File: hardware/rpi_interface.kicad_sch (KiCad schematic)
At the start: 5 parts, among them J14 RPI_Connector, M1 Noctua NF-A4x10

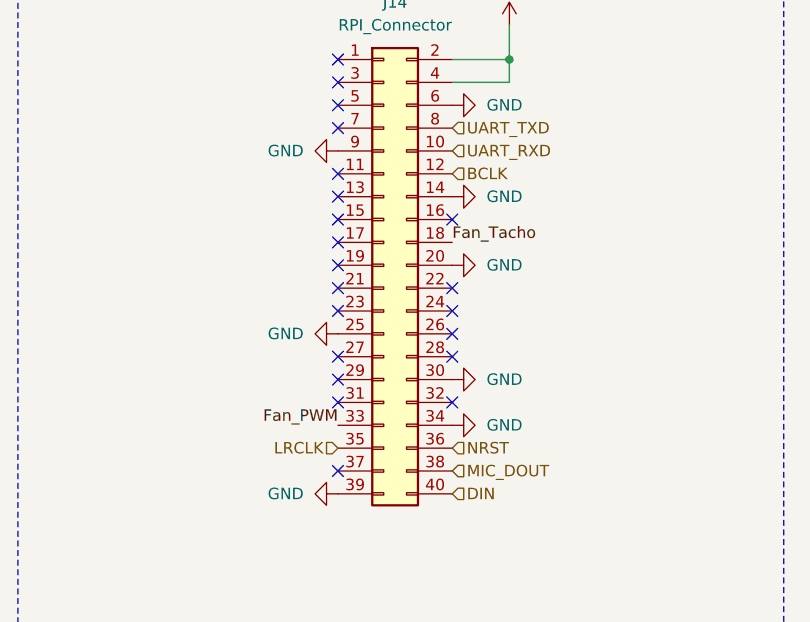
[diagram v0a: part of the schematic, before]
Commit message: schematic update
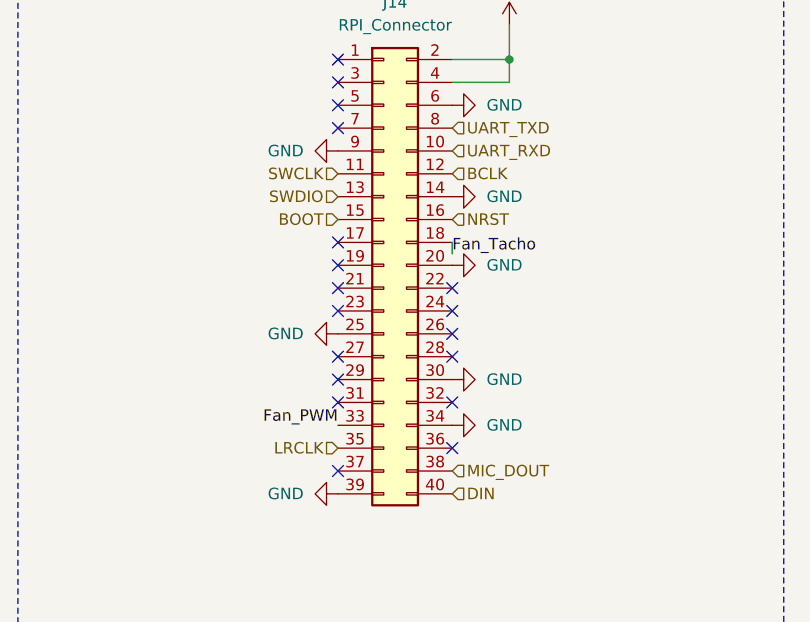
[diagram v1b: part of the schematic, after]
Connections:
- net NRST: now also J14.16 (Pin_16); no longer J14.36 (Pin_36)
- net SWCLK: now reaches J14.11 (Pin_11)
- net SWDIO: now reaches J14.13 (Pin_13)
- net BOOT: now reaches J14.15 (Pin_15)
- no-connect marks 21 -> 18
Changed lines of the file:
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@@
 	)
 	(no_connect
-		(at 142.24 90.17)
+		(at 154.94 120.65)
 	)
 	(no_connect
@@
 	)
 	(no_connect
-		(at 154.94 95.25)
-	)
-	(no_connect
 		(at 142.24 100.33)
 	)
@@
 	)
 	(no_connect
-		(at 142.24 92.71)
-	)
-	(no_connect
 		(at 142.24 123.19)
 	)
@@
 	)
 	(no_connect
-		(at 142.24 95.25)
-	)
-	(no_connect
 		(at 154.94 107.95)
 	)
@@
 	(wire
 		(pts
+			(xy 154.94 99.06) (xy 154.94 97.79)
+		)
+		(stroke
+			(width 0)
+			(type default)
+		)
+	)
+	(wire
+		(pts
 			(xy 209.55 118.11) (xy 212.09 118.11)
 		)
@@
 	)
 	(label "Fan_Tacho"
-		(at 154.94 97.79 0)
+		(at 154.94 99.06 0)
 		(effects
 			(font
@@
 		)
 	)
-	(hierarchical_label "NRST"
+	(hierarchical_label "MIC_DOUT"
 		(shape input)
-		(at 154.94 120.65 0)
+		(at 154.94 123.19 0)
 		(effects
 			(font
@@
 		)
 	)
-	(hierarchical_label "MIC_DOUT"
+	(hierarchical_label "UART_RXD"
 		(shape input)
-		(at 154.94 123.19 0)
+		(at 154.94 87.63 0)
 		(effects
 			(font
@@
 		)
 	)
-	(hierarchical_label "UART_RXD"
+	(hierarchical_label "DIN"
 		(shape input)
-		(at 154.94 87.63 0)
+		(at 154.94 125.73 0)
 		(effects
 			(font
@@
 		)
 	)
-	(hierarchical_label "DIN"
+	(hierarchical_label "SWDIO"
 		(shape input)
-		(at 154.94 125.73 0)
+		(at 142.24 92.71 180)
 		(effects
 			(font
 				(size 1.27 1.27)
 			)
-			(justify left)
+			(justify right)
 		)
 	)
@@
 		)
 	)
+	(hierarchical_label "SWCLK"
+		(shape input)
+		(at 142.24 90.17 180)
+		(effects
+			(font
+				(size 1.27 1.27)
+			)
+			(justify right)
+		)
+	)
 	(hierarchical_label "UART_TXD"
 		(shape input)
@@
 		)
 	)
+	(hierarchical_label "NRST"
+		(shape input)
+		(at 154.94 95.25 0)
+		(effects
+			(font
+				(size 1.27 1.27)
+			)
+			(justify left)
+		)
+	)
+	(hierarchical_label "BOOT"
+		(shape input)
+		(at 142.24 95.25 180)
+		(effects
+			(font
+				(size 1.27 1.27)
+			)
+			(justify right)
+		)
+	)

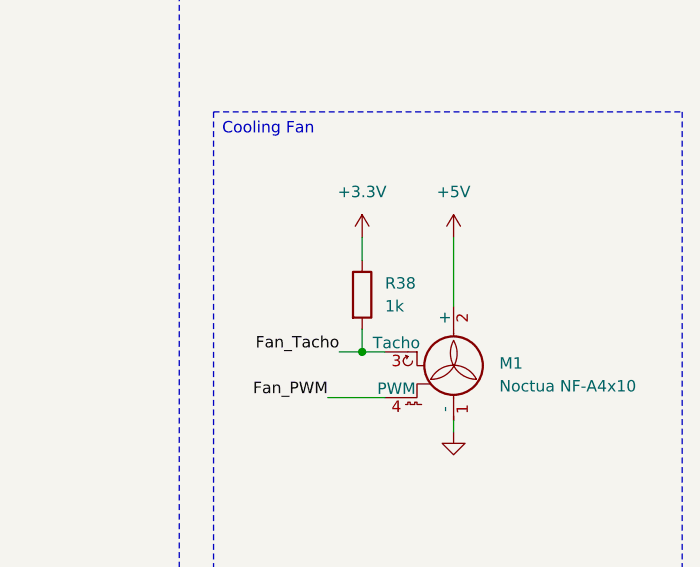
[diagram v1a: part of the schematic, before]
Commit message: replacing components
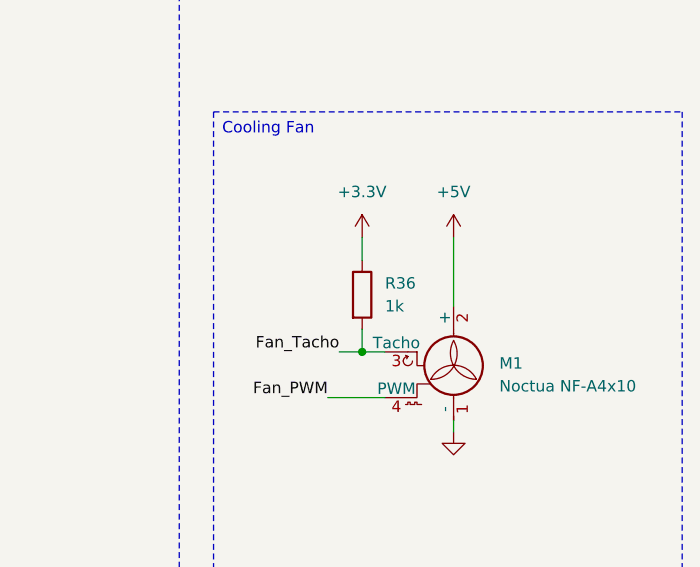
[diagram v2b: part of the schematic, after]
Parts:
- renumbered R38 to R36
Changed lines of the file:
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@@
 		(dnp no)
 		(fields_autoplaced yes)
-		(property "Reference" "#PWR0107"
+		(property "Reference" "#PWR0101"
 			(at 161.29 92.71 0)
 			(hide yes)
@@
 			(project "chromapi_motherboard_v1"
 				(path "/d1a31f26-03e0-43e1-89c1-031fe31befc5/e996aba6-741c-4e73-a7c7-e6548b7ec52f"
-					(reference "#PWR0107")
+					(reference "#PWR0101")
 					(unit 1)
 				)
@@
 		(dnp no)
 		(fields_autoplaced yes)
-		(property "Reference" "#PWR0117"
+		(property "Reference" "#PWR0111"
 			(at 222.25 133.35 0)
 			(hide yes)
@@
 			(project "chromapi_motherboard_v1"
 				(path "/d1a31f26-03e0-43e1-89c1-031fe31befc5/e996aba6-741c-4e73-a7c7-e6548b7ec52f"
-					(reference "#PWR0117")
+					(reference "#PWR0111")
 					(unit 1)
 				)
@@
 		(dnp no)
 		(fields_autoplaced yes)
-		(property "Reference" "#PWR0115"
+		(property "Reference" "#PWR0109"
 			(at 71.12 130.81 0)
 			(hide yes)
@@
 			(project "chromapi_motherboard_v1"
 				(path "/d1a31f26-03e0-43e1-89c1-031fe31befc5/e996aba6-741c-4e73-a7c7-e6548b7ec52f"
-					(reference "#PWR0115")
+					(reference "#PWR0109")
 					(unit 1)
 				)
@@
 		(dnp no)
 		(fields_autoplaced yes)
-		(property "Reference" "#PWR0106"
+		(property "Reference" "#PWR0100"
 			(at 135.89 87.63 0)
 			(hide yes)
@@
 			(project "chromapi_motherboard_v1"
 				(path "/d1a31f26-03e0-43e1-89c1-031fe31befc5/e996aba6-741c-4e73-a7c7-e6548b7ec52f"
-					(reference "#PWR0106")
+					(reference "#PWR0100")
 					(unit 1)
 				)
@@
 		(dnp no)
 		(fields_autoplaced yes)
-		(property "Reference" "R38"
+		(property "Reference" "R36"
 			(at 214.63 110.4899 0)
 			(show_name no)
@@
 			(project "chromapi_motherboard_v1"
 				(path "/d1a31f26-03e0-43e1-89c1-031fe31befc5/e996aba6-741c-4e73-a7c7-e6548b7ec52f"
-					(reference "R38")
+					(reference "R36")
 					(unit 1)
 				)
@@
 		(in_pos_files yes)
 		(dnp no)
-		(property "Reference" "#PWR0111"
+		(property "Reference" "#PWR0105"
 			(at 71.12 111.76 0)
 			(hide yes)
@@
 			(project "chromapi_motherboard_v1"
 				(path "/d1a31f26-03e0-43e1-89c1-031fe31befc5/e996aba6-741c-4e73-a7c7-e6548b7ec52f"
-					(reference "#PWR0111")
+					(reference "#PWR0105")
 					(unit 1)
 				)
@@
 		(dnp no)
 		(fields_autoplaced yes)
-		(property "Reference" "#PWR0116"
+		(property "Reference" "#PWR0110"
 			(at 135.89 125.73 0)
 			(hide yes)
@@
 			(project "chromapi_motherboard_v1"
 				(path "/d1a31f26-03e0-43e1-89c1-031fe31befc5/e996aba6-741c-4e73-a7c7-e6548b7ec52f"
-					(reference "#PWR0116")
+					(reference "#PWR0110")
 					(unit 1)
 				)
@@
 		(dnp no)
 		(fields_autoplaced yes)
-		(property "Reference" "#PWR0104"
+		(property "Reference" "#PWR098"
 			(at 161.29 77.47 0)
 			(hide yes)
@@
 			(project "chromapi_motherboard_v1"
 				(path "/d1a31f26-03e0-43e1-89c1-031fe31befc5/e996aba6-741c-4e73-a7c7-e6548b7ec52f"
-					(reference "#PWR0104")
+					(reference "#PWR098")
 					(unit 1)
 				)
@@
 		(dnp no)
 		(fields_autoplaced yes)
-		(property "Reference" "#PWR0105"
+		(property "Reference" "#PWR099"
 			(at 161.29 82.55 0)
 			(hide yes)
@@
 			(project "chromapi_motherboard_v1"
 				(path "/d1a31f26-03e0-43e1-89c1-031fe31befc5/e996aba6-741c-4e73-a7c7-e6548b7ec52f"
-					(reference "#PWR0105")
+					(reference "#PWR099")
 					(unit 1)
 				)
@@
 		(dnp no)
 		(fields_autoplaced yes)
-		(property "Reference" "#PWR0114"
+		(property "Reference" "#PWR0108"
 			(at 161.29 118.11 0)
 			(hide yes)
@@
 			(project "chromapi_motherboard_v1"
 				(path "/d1a31f26-03e0-43e1-89c1-031fe31befc5/e996aba6-741c-4e73-a7c7-e6548b7ec52f"
-					(reference "#PWR0114")
+					(reference "#PWR0108")
 					(unit 1)
 				)
@@
 		(dnp no)
 		(fields_autoplaced yes)
-		(property "Reference" "#PWR0113"
+		(property "Reference" "#PWR0107"
 			(at 161.29 113.03 0)
 			(hide yes)
@@
 			(project "chromapi_motherboard_v1"
 				(path "/d1a31f26-03e0-43e1-89c1-031fe31befc5/e996aba6-741c-4e73-a7c7-e6548b7ec52f"
-					(reference "#PWR0113")
+					(reference "#PWR0107")
 					(unit 1)
 				)
@@
 		(dnp no)
 		(fields_autoplaced yes)
-		(property "Reference" "#PWR0110"
+		(property "Reference" "#PWR0104"
 			(at 222.25 109.22 0)
 			(hide yes)
@@
 			(project "chromapi_motherboard_v1"
 				(path "/d1a31f26-03e0-43e1-89c1-031fe31befc5/e996aba6-741c-4e73-a7c7-e6548b7ec52f"
-					(reference "#PWR0110")
+					(reference "#PWR0104")
 					(unit 1)
 				)
@@
 		(dnp no)
 		(fields_autoplaced yes)
-		(property "Reference" "#PWR0108"
+		(property "Reference" "#PWR0102"
 			(at 161.29 100.33 0)
 			(hide yes)
@@
 			(project "chromapi_motherboard_v1"
 				(path "/d1a31f26-03e0-43e1-89c1-031fe31befc5/e996aba6-741c-4e73-a7c7-e6548b7ec52f"
-					(reference "#PWR0108")
+					(reference "#PWR0102")
 					(unit 1)
 				)
@@
 		(dnp no)
 		(fields_autoplaced yes)
-		(property "Reference" "#PWR0109"
+		(property "Reference" "#PWR0103"
 			(at 212.09 109.22 0)
 			(hide yes)
@@
 			(project "chromapi_motherboard_v1"
 				(path "/d1a31f26-03e0-43e1-89c1-031fe31befc5/e996aba6-741c-4e73-a7c7-e6548b7ec52f"
-					(reference "#PWR0109")
+					(reference "#PWR0103")
 					(unit 1)
 				)
@@
 		(dnp no)
 		(fields_autoplaced yes)
-		(property "Reference" "#PWR0112"
+		(property "Reference" "#PWR0106"
 			(at 135.89 107.95 0)
 			(hide yes)
@@
 			(project "chromapi_motherboard_v1"
 				(path "/d1a31f26-03e0-43e1-89c1-031fe31befc5/e996aba6-741c-4e73-a7c7-e6548b7ec52f"
-					(reference "#PWR0112")
+					(reference "#PWR0106")
 					(unit 1)
 				)

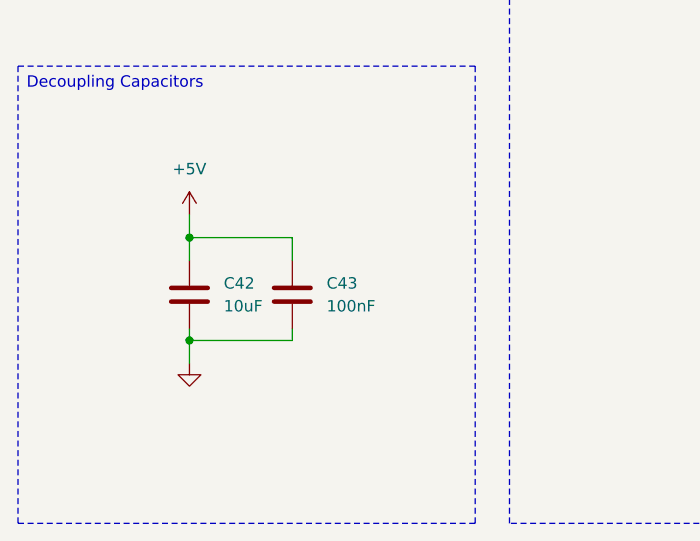
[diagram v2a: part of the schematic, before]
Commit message: schematic update
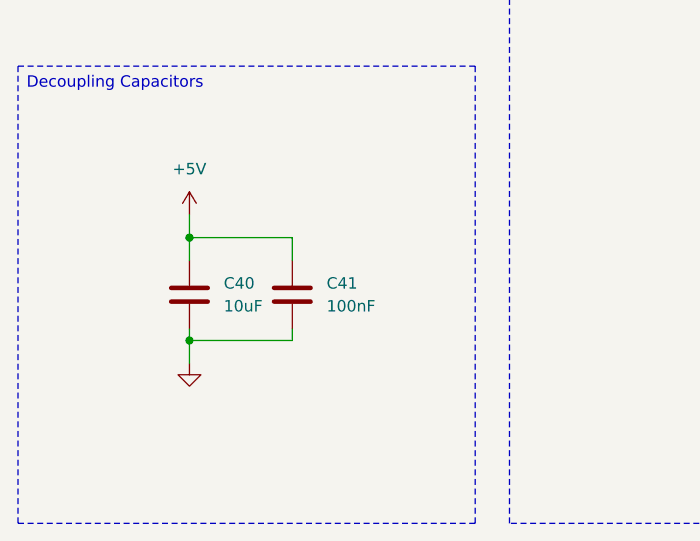
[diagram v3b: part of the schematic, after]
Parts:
- renumbered C42 to C40, C43 to C41
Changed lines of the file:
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@@
 		(dnp no)
 		(fields_autoplaced yes)
-		(property "Reference" "#PWR0101"
+		(property "Reference" "#PWR096"
 			(at 161.29 92.71 0)
 			(hide yes)
@@
 			(project "chromapi_motherboard_v1"
 				(path "/d1a31f26-03e0-43e1-89c1-031fe31befc5/e996aba6-741c-4e73-a7c7-e6548b7ec52f"
-					(reference "#PWR0101")
+					(reference "#PWR096")
 					(unit 1)
 				)
@@
 		(dnp no)
 		(fields_autoplaced yes)
-		(property "Reference" "C43"
+		(property "Reference" "C41"
 			(at 86.36 115.5699 0)
 			(show_name no)
@@
 			(project "chromapi_motherboard_v1"
 				(path "/d1a31f26-03e0-43e1-89c1-031fe31befc5/e996aba6-741c-4e73-a7c7-e6548b7ec52f"
-					(reference "C43")
+					(reference "C41")
 					(unit 1)
 				)
@@
 		(dnp no)
 		(fields_autoplaced yes)
-		(property "Reference" "#PWR0111"
+		(property "Reference" "#PWR0106"
 			(at 222.25 133.35 0)
 			(hide yes)
@@
 			(project "chromapi_motherboard_v1"
 				(path "/d1a31f26-03e0-43e1-89c1-031fe31befc5/e996aba6-741c-4e73-a7c7-e6548b7ec52f"
-					(reference "#PWR0111")
+					(reference "#PWR0106")
 					(unit 1)
 				)
@@
 		(dnp no)
 		(fields_autoplaced yes)
-		(property "Reference" "#PWR0109"
+		(property "Reference" "#PWR0104"
 			(at 71.12 130.81 0)
 			(hide yes)
@@
 			(project "chromapi_motherboard_v1"
 				(path "/d1a31f26-03e0-43e1-89c1-031fe31befc5/e996aba6-741c-4e73-a7c7-e6548b7ec52f"
-					(reference "#PWR0109")
+					(reference "#PWR0104")
 					(unit 1)
 				)
@@
 		(dnp no)
 		(fields_autoplaced yes)
-		(property "Reference" "#PWR0100"
+		(property "Reference" "#PWR095"
 			(at 135.89 87.63 0)
 			(hide yes)
@@
 			(project "chromapi_motherboard_v1"
 				(path "/d1a31f26-03e0-43e1-89c1-031fe31befc5/e996aba6-741c-4e73-a7c7-e6548b7ec52f"
-					(reference "#PWR0100")
+					(reference "#PWR095")
 					(unit 1)
 				)
@@
 		(in_pos_files yes)
 		(dnp no)
-		(property "Reference" "#PWR0105"
+		(property "Reference" "#PWR0100"
 			(at 71.12 111.76 0)
 			(hide yes)
@@
 			(project "chromapi_motherboard_v1"
 				(path "/d1a31f26-03e0-43e1-89c1-031fe31befc5/e996aba6-741c-4e73-a7c7-e6548b7ec52f"
-					(reference "#PWR0105")
+					(reference "#PWR0100")
 					(unit 1)
 				)
@@
 		(dnp no)
 		(fields_autoplaced yes)
-		(property "Reference" "#PWR0110"
+		(property "Reference" "#PWR0105"
 			(at 135.89 125.73 0)
 			(hide yes)
@@
 			(project "chromapi_motherboard_v1"
 				(path "/d1a31f26-03e0-43e1-89c1-031fe31befc5/e996aba6-741c-4e73-a7c7-e6548b7ec52f"
-					(reference "#PWR0110")
+					(reference "#PWR0105")
 					(unit 1)
 				)
@@
 		(dnp no)
 		(fields_autoplaced yes)
-		(property "Reference" "#PWR098"
+		(property "Reference" "#PWR093"
 			(at 161.29 77.47 0)
 			(hide yes)
@@
 			(project "chromapi_motherboard_v1"
 				(path "/d1a31f26-03e0-43e1-89c1-031fe31befc5/e996aba6-741c-4e73-a7c7-e6548b7ec52f"
-					(reference "#PWR098")
+					(reference "#PWR093")
 					(unit 1)
 				)
@@
 		(dnp no)
 		(fields_autoplaced yes)
-		(property "Reference" "#PWR099"
+		(property "Reference" "#PWR094"
 			(at 161.29 82.55 0)
 			(hide yes)
@@
 			(project "chromapi_motherboard_v1"
 				(path "/d1a31f26-03e0-43e1-89c1-031fe31befc5/e996aba6-741c-4e73-a7c7-e6548b7ec52f"
-					(reference "#PWR099")
+					(reference "#PWR094")
 					(unit 1)
 				)
@@
 		(dnp no)
 		(fields_autoplaced yes)
-		(property "Reference" "#PWR0108"
+		(property "Reference" "#PWR0103"
 			(at 161.29 118.11 0)
 			(hide yes)
@@
 			(project "chromapi_motherboard_v1"
 				(path "/d1a31f26-03e0-43e1-89c1-031fe31befc5/e996aba6-741c-4e73-a7c7-e6548b7ec52f"
-					(reference "#PWR0108")
+					(reference "#PWR0103")
 					(unit 1)
 				)
@@
 		(dnp no)
 		(fields_autoplaced yes)
-		(property "Reference" "#PWR0107"
+		(property "Reference" "#PWR0102"
 			(at 161.29 113.03 0)
 			(hide yes)
@@
 			(project "chromapi_motherboard_v1"
 				(path "/d1a31f26-03e0-43e1-89c1-031fe31befc5/e996aba6-741c-4e73-a7c7-e6548b7ec52f"
-					(reference "#PWR0107")
+					(reference "#PWR0102")
 					(unit 1)
 				)
@@
 		(dnp no)
 		(fields_autoplaced yes)
-		(property "Reference" "#PWR0104"
+		(property "Reference" "#PWR099"
 			(at 222.25 109.22 0)
 			(hide yes)
@@
 			(project "chromapi_motherboard_v1"
 				(path "/d1a31f26-03e0-43e1-89c1-031fe31befc5/e996aba6-741c-4e73-a7c7-e6548b7ec52f"
-					(reference "#PWR0104")
+					(reference "#PWR099")
 					(unit 1)
 				)
@@
 		(dnp no)
 		(fields_autoplaced yes)
-		(property "Reference" "#PWR0102"
+		(property "Reference" "#PWR097"
 			(at 161.29 100.33 0)
 			(hide yes)
@@
 			(project "chromapi_motherboard_v1"
 				(path "/d1a31f26-03e0-43e1-89c1-031fe31befc5/e996aba6-741c-4e73-a7c7-e6548b7ec52f"
-					(reference "#PWR0102")
+					(reference "#PWR097")
 					(unit 1)
 				)
@@
 		(dnp no)
 		(fields_autoplaced yes)
-		(property "Reference" "#PWR0103"
+		(property "Reference" "#PWR098"
 			(at 212.09 109.22 0)
 			(hide yes)
@@
 			(project "chromapi_motherboard_v1"
 				(path "/d1a31f26-03e0-43e1-89c1-031fe31befc5/e996aba6-741c-4e73-a7c7-e6548b7ec52f"
-					(reference "#PWR0103")
+					(reference "#PWR098")
 					(unit 1)
 				)
@@
 		(dnp no)
 		(fields_autoplaced yes)
-		(property "Reference" "#PWR0106"
+		(property "Reference" "#PWR0101"
 			(at 135.89 107.95 0)
 			(hide yes)
@@
 			(project "chromapi_motherboard_v1"
 				(path "/d1a31f26-03e0-43e1-89c1-031fe31befc5/e996aba6-741c-4e73-a7c7-e6548b7ec52f"
-					(reference "#PWR0106")
+					(reference "#PWR0101")
 					(unit 1)
 				)
@@
 		(dnp no)
 		(fields_autoplaced yes)
-		(property "Reference" "C42"
+		(property "Reference" "C40"
 			(at 74.93 115.5699 0)
 			(show_name no)
@@
 			(project "chromapi_motherboard_v1"
 				(path "/d1a31f26-03e0-43e1-89c1-031fe31befc5/e996aba6-741c-4e73-a7c7-e6548b7ec52f"
-					(reference "C42")
+					(reference "C40")
 					(unit 1)
 				)
